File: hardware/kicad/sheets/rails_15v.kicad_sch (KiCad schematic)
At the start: 31 parts, among them U20 ADP5071AREZ, U21 ADP7142AUJZ, U22 ADP7182AUJZ

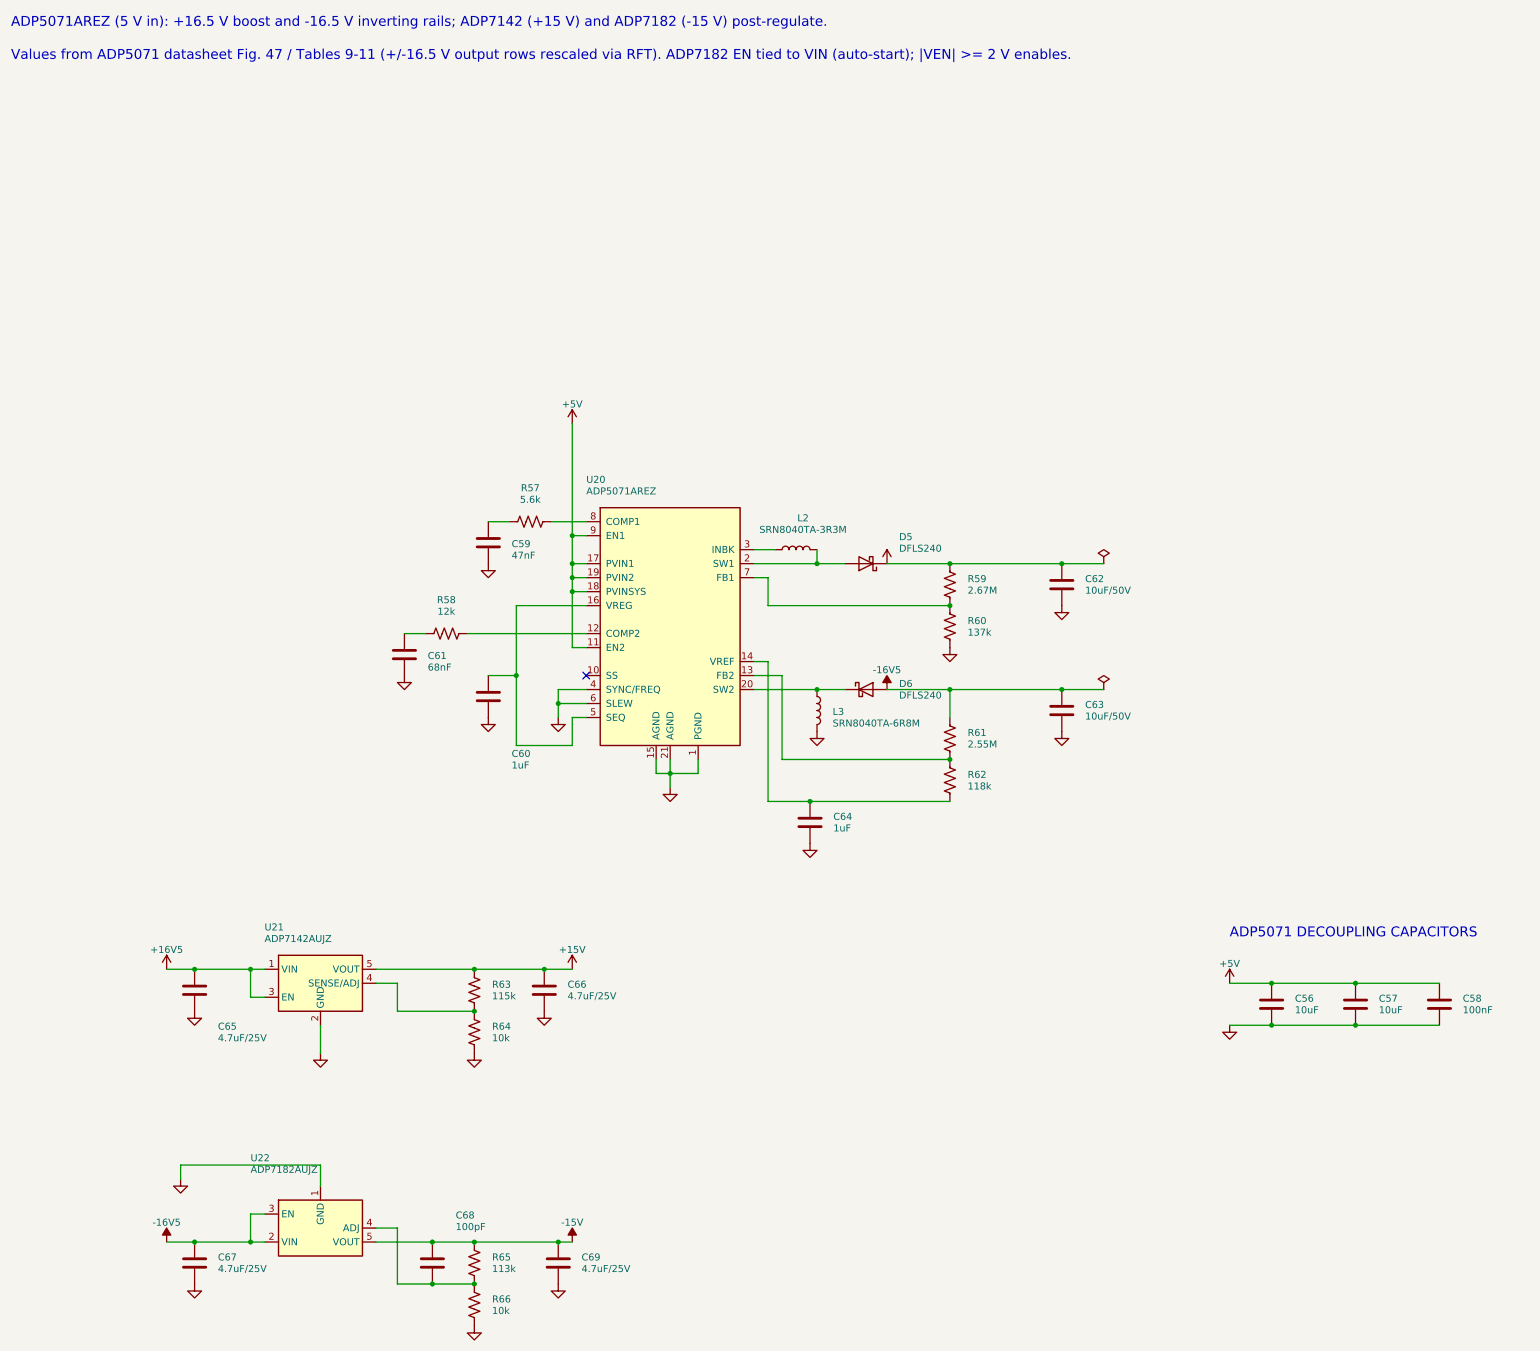
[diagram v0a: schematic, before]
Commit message: Put supply pins on top and grounds on the bottom of IC symbols; flake8-clean Python
Schematic: re-laid out pins on U2, U3, U6, U7, U11, U14, U17-U20, U22-U24
and PS1 (supply on top, ground/strap pins on the bottom edge) via custom
`cryocooler:` symbols (make_lib.from_stock) and a gnd_bus helper; U18/U2
use mirroring instead of a 180 degree rotation. Nets are unchanged (ERC 0,
117/117 datasheet rules, PCB nets still match). Text placement now shows
every power-symbol name, avoids wires, and uses a realistic character width.

Python: black -l 79 -S plus manual wrapping so hardware/kicad and scripts/
pass flake8; add .flake8.

Co-Authored-By: Claude Sonnet 5.5 <noreply@anthropic.com>
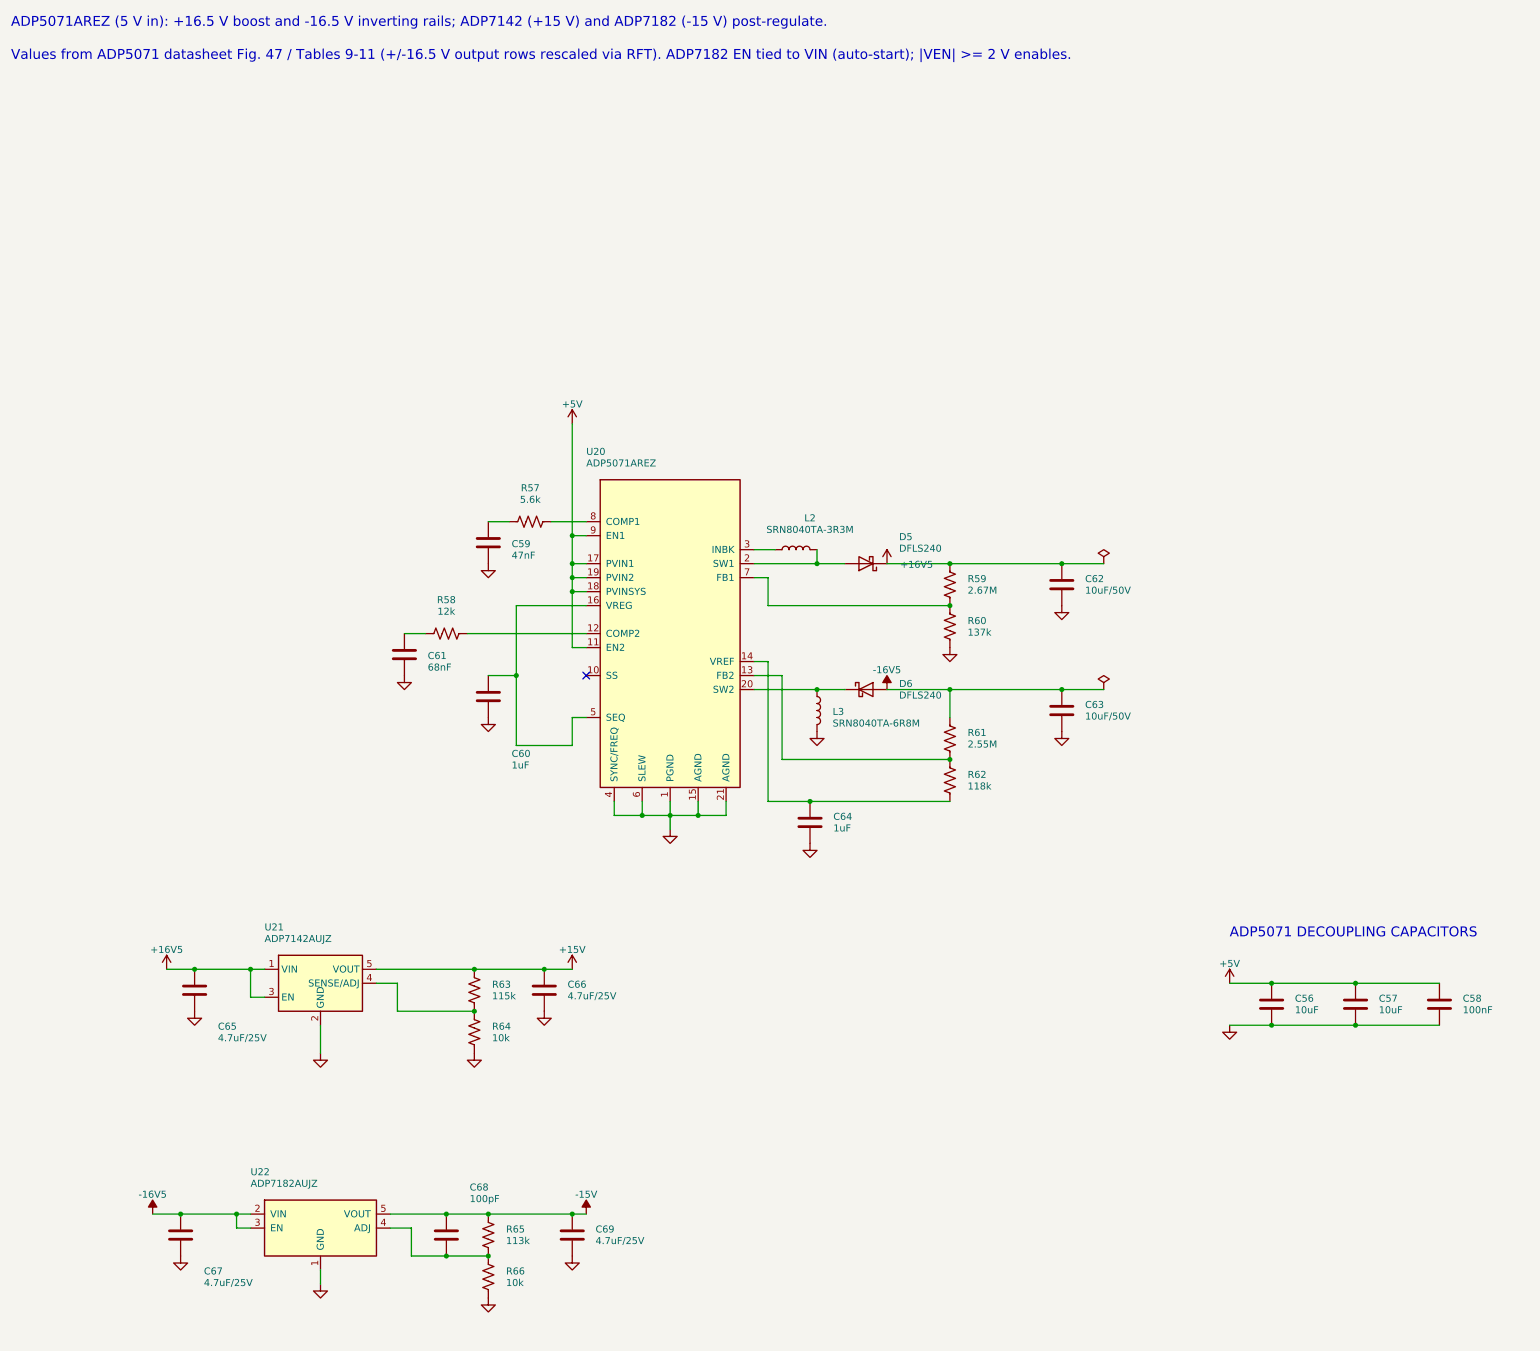
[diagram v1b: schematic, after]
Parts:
- removed C60: 1uF, Capacitor_SMD:C_0805_2012Metric, symbol Device:C
- removed C63: 10uF/50V, Capacitor_SMD:C_1210_3225Metric, symbol Device:C
- removed D5: DFLS240, Diode_SMD:D_PowerDI-123, symbol Device:D_Schottky
- removed R60: 137k, Resistor_SMD:R_0603_1608Metric, symbol Device:R_US
- removed R61: 2.55M, Resistor_SMD:R_0603_1608Metric, symbol Device:R_US
- removed R64, R66: 10k, Resistor_SMD:R_0603_1608Metric, symbol Device:R_US
- removed U21: ADP7142AUJZ, Package_TO_SOT_SMD:TSOT-23-5, symbol Regulator_Linear:ADP7142AUJZ
- removed U22: ADP7182AUJZ, Package_TO_SOT_SMD:TSOT-23-5, symbol Regulator_Linear:ADP7182AUJZ
- added C58: 100nF, Capacitor_SMD:C_0603_1608Metric, symbol Device:C
- added C61: 68nF, Capacitor_SMD:C_1206_3216Metric, symbol Device:C
- added C65, C67: 4.7uF/25V, Capacitor_SMD:C_1206_3216Metric, symbol Device:C
- added D6: DFLS240, Diode_SMD:D_PowerDI-123, symbol Device:D_Schottky
- added R59: 2.67M, Resistor_SMD:R_0603_1608Metric, symbol Device:R_US
- added R62: 118k, Resistor_SMD:R_0603_1608Metric, symbol Device:R_US
- added R63: 115k, Resistor_SMD:R_0603_1608Metric, symbol Device:R_US
- added U20: ADP5071AREZ, Package_SO:ETSSOP-20-1EP_4.4x6.5mm_P0.65mm_EP3x4.2mm, symbol cryocooler:ADP5071AREZ
- C56: renamed from U20; value ADP5071AREZ -> 10uF; footprint Package_SO:ETSSOP-20-1EP_4.4x6.5mm_P0.65mm_EP3x4.2mm -> Capacitor_SMD:C_0805_2012Metric; symbol Regulator_Switching:ADP5071AREZ -> Device:C
- C59: renamed from C56; value 10uF -> 47nF; footprint Capacitor_SMD:C_0805_2012Metric -> Capacitor_SMD:C_1206_3216Metric
- C60: renamed from C58; value 100nF -> 1uF; footprint Capacitor_SMD:C_0603_1608Metric -> Capacitor_SMD:C_0805_2012Metric
- C63: renamed from D6; value DFLS240 -> 10uF/50V; footprint Diode_SMD:D_PowerDI-123 -> Capacitor_SMD:C_1210_3225Metric; symbol Device:D_Schottky -> Device:C
- D5: renamed from C61; value 68nF -> DFLS240; footprint Capacitor_SMD:C_1206_3216Metric -> Diode_SMD:D_PowerDI-123; symbol Device:C -> Device:D_Schottky
- L2: renamed from R58; value 12k -> SRN8040TA-3R3M; footprint Resistor_SMD:R_0603_1608Metric -> Inductor_SMD:L_Bourns_SRN8040TA; symbol Device:R_US -> Device:L
- L3: renamed from R59; value 2.67M -> SRN8040TA-6R8M; footprint Resistor_SMD:R_0603_1608Metric -> Inductor_SMD:L_Bourns_SRN8040TA; symbol Device:R_US -> Device:L
- R58: renamed from C59; value 47nF -> 12k; footprint Capacitor_SMD:C_1206_3216Metric -> Resistor_SMD:R_0603_1608Metric; symbol Device:C -> Device:R_US
- R60: renamed from L2; value SRN8040TA-3R3M -> 137k; footprint Inductor_SMD:L_Bourns_SRN8040TA -> Resistor_SMD:R_0603_1608Metric; symbol Device:L -> Device:R_US
- R61: renamed from L3; value SRN8040TA-6R8M -> 2.55M; footprint Inductor_SMD:L_Bourns_SRN8040TA -> Resistor_SMD:R_0603_1608Metric; symbol Device:L -> Device:R_US
- R64: renamed from C65; value 4.7uF/25V -> 10k; footprint Capacitor_SMD:C_1206_3216Metric -> Resistor_SMD:R_0603_1608Metric; symbol Device:C -> Device:R_US
- R66: renamed from C67; value 4.7uF/25V -> 10k; footprint Capacitor_SMD:C_1206_3216Metric -> Resistor_SMD:R_0603_1608Metric; symbol Device:C -> Device:R_US
- U21: renamed from R62; value 118k -> ADP7142AUJZ; footprint Resistor_SMD:R_0603_1608Metric -> Package_TO_SOT_SMD:TSOT-23-5; symbol Device:R_US -> Regulator_Linear:ADP7142AUJZ
- U22: renamed from R63; value 115k -> ADP7182AUJZ; footprint Resistor_SMD:R_0603_1608Metric -> Package_TO_SOT_SMD:TSOT-23-5; symbol Device:R_US -> cryocooler:ADP7182AUJZ
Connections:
- net +15V: now also U21.5 (VOUT), R63.1; no longer U22.1
- net +16V5: now also D5.1 (K), U21.1 (VIN), U21.3 (EN), C65.1, R59.1; no longer L3.1, R64.1
- net +5V: now also C56.1, C58.1, U20.11 (EN2), U20.17 (PVIN1), U20.18 (PVINSYS), U20.19 (PVIN2), U20.9 (EN1); no longer C56.11 (EN2), C56.17 (PVIN1), C56.18 (PVINSYS), C56.19 (PVIN2), C56.9 (EN1), C59.1, C60.1
- net -15V: now also U22.5 (VOUT)
- net -16V5: now also C63.1, R61.1, U22.2 (VIN), U22.3 (EN), C67.1, D6.2 (A); no longer C63.2 (A), R66.1
- net GND: now also C56.2, C63.2, L3.2, R60.2, U21.2 (GND), U22.1 (GND), C58.2, C61.2, C65.2, C67.2, U20.1 (PGND), U20.15 (AGND), U20.21 (AGND), U20.4 (SYNC/FREQ), U20.6 (SLEW); no longer C56.1 (PGND), C56.15 (AGND), C56.21 (AGND), C56.4 (SYNC/FREQ), C56.6 (SLEW), D5.2, R58.2, R61.2
- net at L2.1: now also U20.3 (INBK); no longer D5.1
- net at L2.2: now also D5.2 (A), U20.2 (SW1); no longer C56.12 (COMP2)
- net at R60.1: now also R59.2, U20.7 (FB1); no longer C56.3 (INBK)
- net at C68.2, R65.2: now also R66.1, U22.4 (ADJ)
- net at R57.1: now also C59.1; no longer R58.1
- net at R57.2: now also U20.8 (COMP1); no longer C56.8 (COMP1)
- new net: R61.2, R62.1, U20.13 (FB2)
- new net: C64.1, R62.2, U20.14 (VREF)
- new net: C61.1, R58.1
- new net: R58.2, U20.12 (COMP2)
- new net: C60.1, U20.16 (VREG), U20.5 (SEQ)
- new net: R63.2, R64.1, U21.4 (SENSE/ADJ)
- new net: D6.1 (K), L3.1, U20.20 (SW2)
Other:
- moved on the sheet: C59, C60

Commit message: KiCad schematic: INA239, ADS1220, SC18IS604 bridge, relay driver, test points
- system_current: INA237 -> INA239 (SPI, CS GPIO3) with the 49.9 ohm / 470 nF
  input filter, power LED and ALERT LED; VBUS shares the filtered IN- node.
- cold_head: ADS122C04 -> ADS1220 (SPI, CS GPIO44).
- i2c_bridge (new): SC18IS604 SPI-to-I2C bridge for the EMC2303, with a
  74LVC1G125 gating its MISO onto the shared bus.
- compressor_relay (new): GPIO16 high-side switch sharing one generator
  function with the amplifier REM switch.
- debug (new): about 40 test points and rail LEDs (the isolated rail LED
  returns to ISO_GND).
- ISO7741 -> ACS37800 SPI lines are straight wires (pins reordered on the
  symbol); USB_VBUS is one wire plus a naming label.
- Custom symbols for INA239, ADS1220, SC18IS604; datasheet rules 117 -> 162;
  GPIO map checks updated. ERC 0.

Co-Authored-By: Claude Sonnet 5.5 <noreply@anthropic.com>
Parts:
- removed C59: 47nF, Capacitor_SMD:C_1206_3216Metric, symbol Device:C
- removed C62: 10uF/50V, Capacitor_SMD:C_1210_3225Metric, symbol Device:C
- removed C64: 1uF, Capacitor_SMD:C_0805_2012Metric, symbol Device:C
- removed C66, C69: 4.7uF/25V, Capacitor_SMD:C_1206_3216Metric, symbol Device:C
- removed C68: 100pF, Capacitor_SMD:C_1206_3216Metric, symbol Device:C
- removed L2: SRN8040TA-3R3M, Inductor_SMD:L_Bourns_SRN8040TA, symbol Device:L
- added C56, C57: 10uF, Capacitor_SMD:C_0805_2012Metric, symbol Device:C
- added D5, D6: DFLS240, Diode_SMD:D_PowerDI-123, symbol Device:D_Schottky
- added R56: 12k, Resistor_SMD:R_0603_1608Metric, symbol Device:R_US
- added R62: 10k, Resistor_SMD:R_0603_1608Metric, symbol Device:R_US
- added R63: 113k, Resistor_SMD:R_0603_1608Metric, symbol Device:R_US
- C59: renamed from C57; value 10uF -> 47nF; footprint Capacitor_SMD:C_0805_2012Metric -> Capacitor_SMD:C_1206_3216Metric
- C60: renamed from R57; value 5.6k -> 1uF; footprint Resistor_SMD:R_0603_1608Metric -> Capacitor_SMD:C_0805_2012Metric; symbol Device:R_US -> Device:C
- C61: renamed from C60; value 1uF -> 68nF; footprint Capacitor_SMD:C_0805_2012Metric -> Capacitor_SMD:C_1206_3216Metric
- C62: renamed from R59; value 2.67M -> 10uF/50V; footprint Resistor_SMD:R_0603_1608Metric -> Capacitor_SMD:C_1210_3225Metric; symbol Device:R_US -> Device:C
- C64: renamed from R62; value 118k -> 1uF; footprint Resistor_SMD:R_0603_1608Metric -> Capacitor_SMD:C_0805_2012Metric; symbol Device:R_US -> Device:C
- C66: renamed from R63; value 115k -> 4.7uF/25V; footprint Resistor_SMD:R_0603_1608Metric -> Capacitor_SMD:C_1206_3216Metric; symbol Device:R_US -> Device:C
- C68: renamed from R65; value 113k -> 100pF; footprint Resistor_SMD:R_0603_1608Metric -> Capacitor_SMD:C_1206_3216Metric; symbol Device:R_US -> Device:C
- C69: renamed from R66; value 10k -> 4.7uF/25V; footprint Resistor_SMD:R_0603_1608Metric -> Capacitor_SMD:C_1206_3216Metric; symbol Device:R_US -> Device:C
- L2: renamed from C61; value 68nF -> SRN8040TA-3R3M; footprint Capacitor_SMD:C_1206_3216Metric -> Inductor_SMD:L_Bourns_SRN8040TA; symbol Device:C -> Device:L
- R55: renamed from C56; value 10uF -> 5.6k; footprint Capacitor_SMD:C_0805_2012Metric -> Resistor_SMD:R_0603_1608Metric; symbol Device:C -> Device:R_US
- R57: renamed from D5; value DFLS240 -> 2.67M; footprint Diode_SMD:D_PowerDI-123 -> Resistor_SMD:R_0603_1608Metric; symbol Device:D_Schottky -> Device:R_US
- R58: value 12k -> 137k
- R59: renamed from D6; value DFLS240 -> 2.55M; footprint Diode_SMD:D_PowerDI-123 -> Resistor_SMD:R_0603_1608Metric; symbol Device:D_Schottky -> Device:R_US
- R60: value 137k -> 118k
- R61: value 2.55M -> 115k
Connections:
- net +15V: now also R61.1
- net +16V5: now also D5.1 (K)
- net +5V: now also C56.1, C57.1; no longer C59.1, R55.1
- net -15V: now also C69.1, R63.1
- net -16V5: now also R59.1, D6.2 (A); no longer R59.2 (A), R61.1
- net GND: now also C60.2, C62.2, C64.2, C66.2, R58.2, C56.2, C57.2, R62.2; no longer L2.2, R55.2, R60.2
- net at C60.1: now also U20.16 (VREG), U20.5 (SEQ)
- net at U20.3 (INBK): now also L2.1
- net at U20.2 (SW1): now also L2.2, D5.2 (A); no longer R57.2 (A)
- net at U20.14 (VREF): now also C64.1, R60.2; no longer C64.2
- net at C68.2, U22.4 (ADJ): now also R64.1, R63.2; no longer C69.1
- net at U20.8 (COMP1): now also R55.2; no longer C60.2
- net at R58.1: now also R57.2, U20.7 (FB1); no longer L2.1
- net at U20.12 (COMP2): now also R56.2; no longer R58.2
- net at L3.1, U20.20 (SW2): now also D6.1 (K); no longer R59.1 (K)
- new net: C61.1, R56.1
- new net: C59.1, R55.1
- new net: R59.2, R60.1, U20.13 (FB2)
- new net: R61.2, R62.1, U21.4 (SENSE/ADJ)
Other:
- moved on the sheet: C59, C61
